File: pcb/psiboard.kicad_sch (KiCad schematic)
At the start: 11 parts, among them J2 BAT+, J3 BAT-

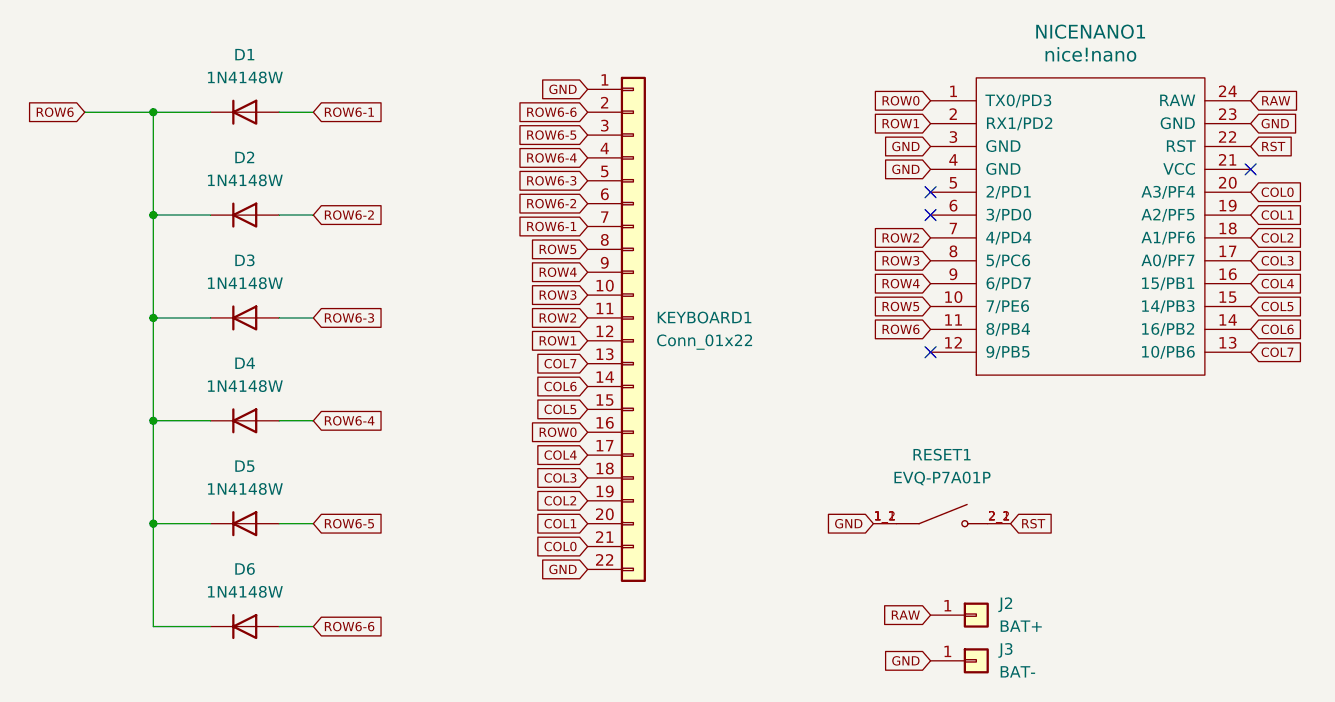
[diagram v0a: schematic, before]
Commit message: Hand-route keyboard to simplify layout
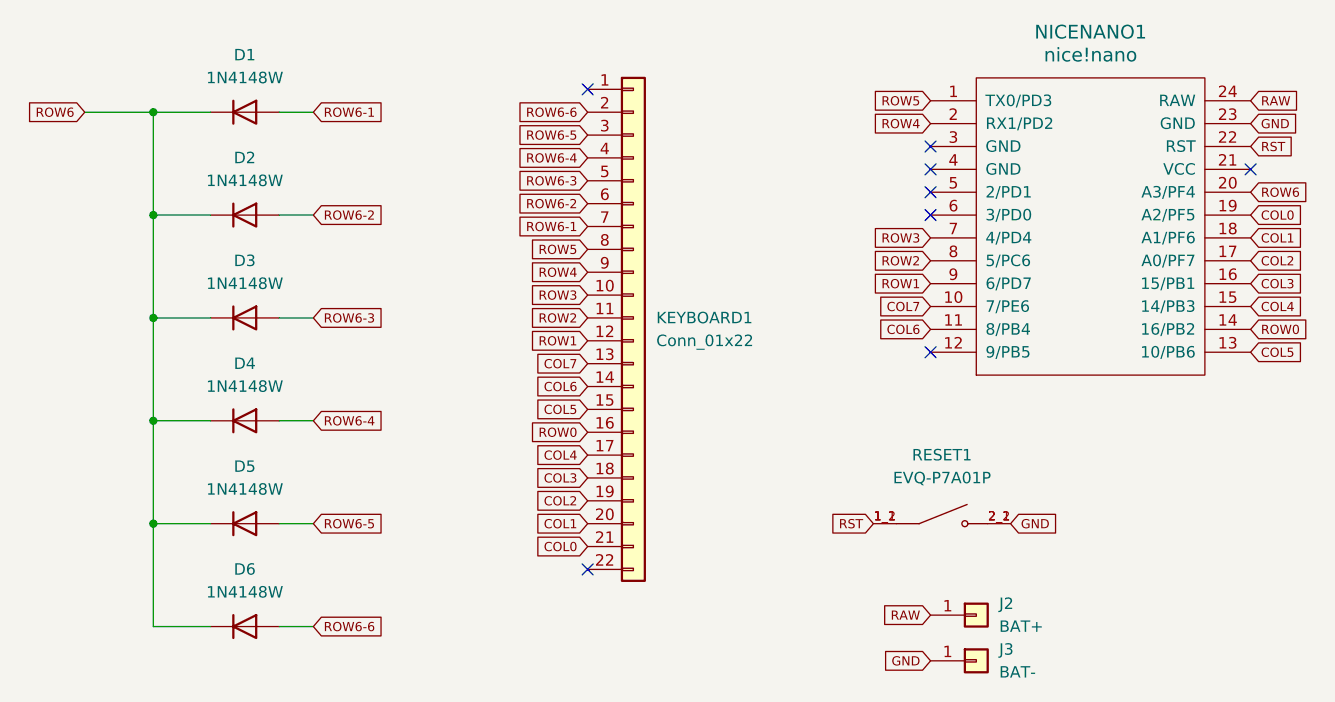
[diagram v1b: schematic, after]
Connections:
- net COL0: now also NICENANO1.19 (A2/PF5); no longer NICENANO1.20 (A3/PF4)
- net COL1: now also NICENANO1.18 (A1/PF6); no longer NICENANO1.19 (A2/PF5)
- net COL2: now also NICENANO1.17 (A0/PF7); no longer NICENANO1.18 (A1/PF6)
- net COL3: now also NICENANO1.16 (15/PB1); no longer NICENANO1.17 (A0/PF7)
- net COL4: now also NICENANO1.15 (14/PB3); no longer NICENANO1.16 (15/PB1)
- net COL5: now also NICENANO1.13 (10/PB6); no longer NICENANO1.15 (14/PB3)
- net COL6: now also NICENANO1.11 (8/PB4); no longer NICENANO1.14 (16/PB2)
- net COL7: now also NICENANO1.10 (7/PE6); no longer NICENANO1.13 (10/PB6)
- net GND: now also RESET1.2_1, RESET1.2_2; no longer KEYBOARD1.1 (Pin_1), KEYBOARD1.22 (Pin_22), NICENANO1.3 (GND), NICENANO1.4 (GND), RESET1.1_1, RESET1.1_2
- net ROW0: now also NICENANO1.14 (16/PB2); no longer NICENANO1.1 (TX0/PD3)
- net ROW1: now also NICENANO1.9 (6/PD7); no longer NICENANO1.2 (RX1/PD2)
- net ROW2: now also NICENANO1.8 (5/PC6); no longer NICENANO1.7 (4/PD4)
- net ROW3: now also NICENANO1.7 (4/PD4); no longer NICENANO1.8 (5/PC6)
- net ROW4: now also NICENANO1.2 (RX1/PD2); no longer NICENANO1.9 (6/PD7)
- net ROW5: now also NICENANO1.1 (TX0/PD3); no longer NICENANO1.10 (7/PE6)
- net ROW6: now also NICENANO1.20 (A3/PF4); no longer NICENANO1.11 (8/PB4)
- net RST: now also RESET1.1_1, RESET1.1_2; no longer RESET1.2_1, RESET1.2_2
- no-connect marks 4 -> 8

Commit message: Latest iteration
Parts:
- KEYBOARD1: footprint 22-pin molex:CON_524352271_MOL -> 22-pin molex (bottom):CON_524372271_MOL
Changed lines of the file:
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@@
 			)
 		)
-		(property "Footprint" "22-pin molex:CON_524352271_MOL"
+		(property "Footprint" "22-pin molex (bottom):CON_524372271_MOL"
 			(at 91.44 58.42 0)
 			(effects

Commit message: Add ground plane
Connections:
- net GND: now also NICENANO1.3 (GND), NICENANO1.4 (GND)
- no-connect marks 8 -> 6
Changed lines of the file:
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@@
-	)
-	(no_connect
-		(at 124.46 39.37)
 	)
 	(no_connect
@@
 	)
 	(no_connect
-		(at 124.46 41.91)
-	)
-	(no_connect
 		(at 160.02 41.91)
 	)
@@
 		)
 	)
+	(global_label "GND"
+		(shape input)
+		(at 124.46 39.37 180)
+		(fields_autoplaced yes)
+		(effects
+			(font
+				(size 1.016 1.016)
+			)
+			(justify right)
+		)
+		(property "Intersheetrefs" "${INTERSHEET_REFS}"
+			(at 117.6043 39.37 0)
+			(effects
+				(font
+					(size 1.27 1.27)
+				)
+				(justify right)
+				(hide yes)
+			)
+		)
+	)
 	(global_label "ROW5"
 		(shape input)
@@
 			(effects
 				(font
+					(size 1.27 1.27)
+				)
+				(justify right)
+				(hide yes)
+			)
+		)
+	)
+	(global_label "GND"
+		(shape input)
+		(at 124.46 41.91 180)
+		(fields_autoplaced yes)
+		(effects
+			(font
+				(size 1.016 1.016)
+			)
+			(justify right)
+		)
+		(property "Intersheetrefs" "${INTERSHEET_REFS}"
+			(at 117.6043 41.91 0)
+			(effects
+				(font
